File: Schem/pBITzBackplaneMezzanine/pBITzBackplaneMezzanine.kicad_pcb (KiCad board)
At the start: 4 copper layers, 139 x 130 mm, 54 parts, among them J1 USB3_A_Stacked, J2 Conn_01x04, J3 Conn_01x04, J4 10067847-001RLF, J5 FH69-60S-0.5SH, J6 pBITzBus, J7 FH69-60S-0.5SH, SW1 SW_Coded_SH-7030, SW2 SW_Coded_SH-7030, U1 FE1.1S-BSOP28BCN, U2 MAX3421EETJ_T, U3 CD74HC4050M96, U4 CD74HC4050M96, U5 74HC688, U6 74HC688, Y1 ABL-12.000MHZ-B2, Y2 ABL-12.000MHZ-B2

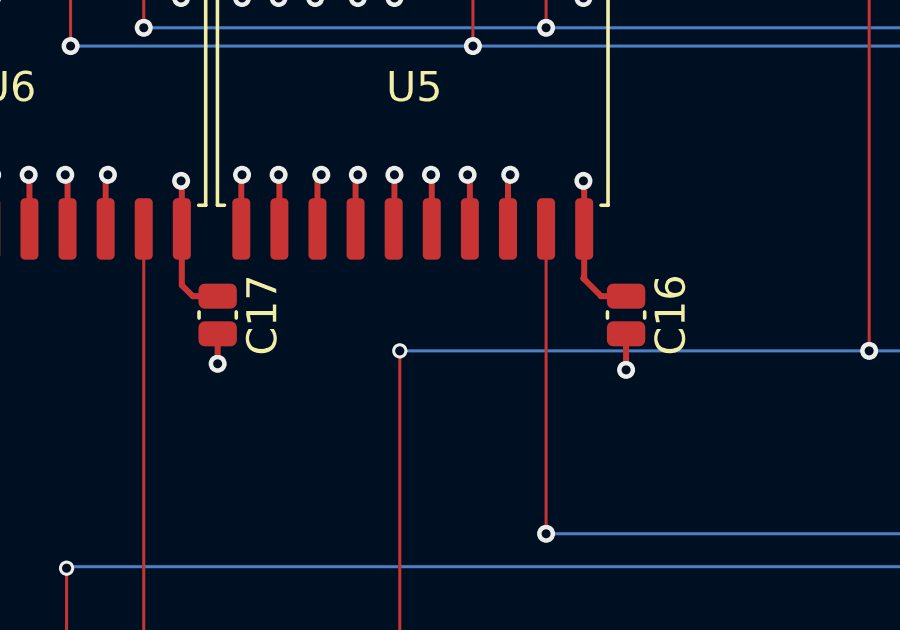
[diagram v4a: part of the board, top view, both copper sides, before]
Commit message: Small errors in BOM
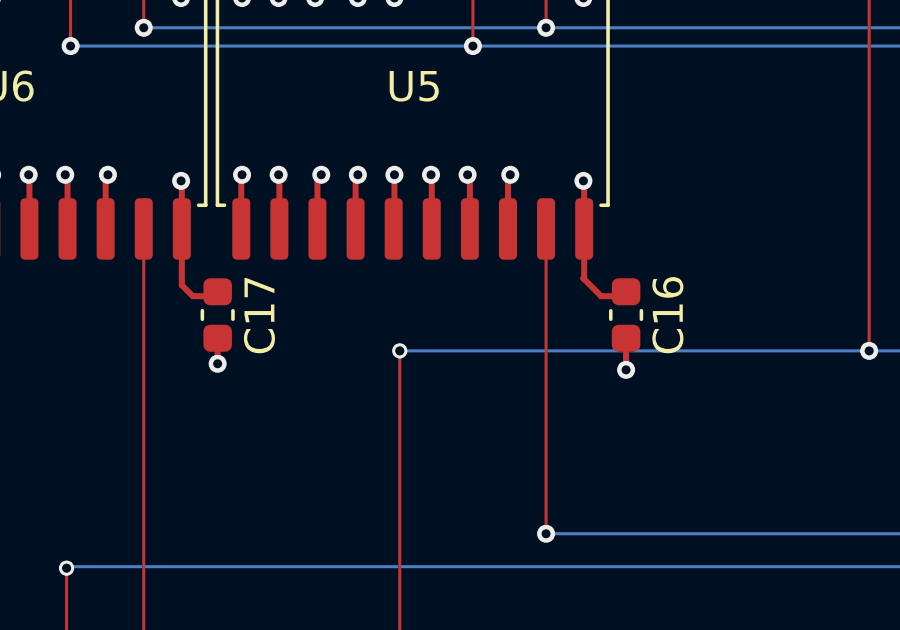
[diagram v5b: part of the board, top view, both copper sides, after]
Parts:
- C16, C17: footprint Capacitor_SMD:C_0504_1310Metric_Pad0.83x1.28mm_HandSolder -> Capacitor_SMD:C_0603_1608Metric
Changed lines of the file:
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@@
 		)
 	)
-	(footprint "Capacitor_SMD:C_0504_1310Metric_Pad0.83x1.28mm_HandSolder"
+	(footprint "Capacitor_SMD:C_0603_1608Metric"
 		(layer "F.Cu")
 		(at 273.747 177.5724 -90)
-		(descr "Capacitor SMD 0504 (1310 Metric), square (rectangular) end terminal, IPC-7351 nominal with elongated pad for handsoldering. (Body size source: IPC-SM-782 page 76, https://www.pcb-3d.com/wordpress/wp-content/uploads/ipc-sm-782a_amendment_1_and_2.pdf), generated with kicad-footprint-generator")
-		(tags "capacitor handsolder")
+		(descr "Capacitor SMD 0603 (1608 Metric), square (rectangular) end terminal, IPC-7351 nominal, (Body size source: IPC-SM-782 page 76, https://www.pcb-3d.com/wordpress/wp-content/uploads/ipc-sm-782a_amendment_1_and_2.pdf), generated with kicad-footprint-generator")
+		(tags "capacitor")
 		(property "Reference" "C17"
-			(at 0 -1.49 270)
+			(at 0 -1.43 270)
 			(layer "F.SilkS")
 			(effects
@@
 		)
 		(property "Value" "100n"
-			(at 0 1.49 270)
+			(at 0 1.43 270)
 			(layer "F.Fab")
 			(effects
@@
 				(font
 					(size 1.27 1.27)
+					(thickness 0.15)
+				)
+			)
+		)
+		(property "MANUFACTURER_PART_NUMBER" "C0603C104K5RACTU"
+			(at 0 0 270)
+			(unlocked yes)
+			(layer "F.Fab")
+			(hide yes)
+			(effects
+				(font
+					(size 1 1)
 					(thickness 0.15)
 				)
@@
 		(attr smd)
 		(fp_line
-			(start -0.101969 0.62)
-			(end 0.101969 0.62)
+			(start -0.14058 0.51)
+			(end 0.14058 0.51)
 			(stroke
 				(width 0.12)
@@
 		)
 		(fp_line
-			(start -0.101969 -0.62)
-			(end 0.101969 -0.62)
+			(start -0.14058 -0.51)
+			(end 0.14058 -0.51)
 			(stroke
 				(width 0.12)
@@
 		)
 		(fp_rect
-			(start -1.2 -0.79)
-			(end 1.2 0.79)
+			(start -1.48 -0.73)
+			(end 1.48 0.73)
 			(stroke
 				(width 0.05)
@@
 		)
 		(fp_rect
-			(start -0.585 -0.51)
-			(end 0.585 0.51)
+			(start -0.8 -0.4)
+			(end 0.8 0.4)
 			(stroke
 				(width 0.1)
@@
 			(effects
 				(font
-					(size 0.29 0.29)
-					(thickness 0.04)
+					(size 0.4 0.4)
+					(thickness 0.06)
 				)
 			)
 		)
 		(pad "1" smd roundrect
-			(at -0.6275 0 270)
-			(size 0.835 1.28)
+			(at -0.775 0 270)
+			(size 0.9 0.95)
 			(layers "F.Cu" "F.Mask" "F.Paste")
 			(roundrect_rratio 0.25)
@@
 		)
 		(pad "2" smd roundrect
-			(at 0.6275 0 270)
-			(size 0.835 1.28)
+			(at 0.775 0 270)
+			(size 0.9 0.95)
 			(layers "F.Cu" "F.Mask" "F.Paste")
 			(roundrect_rratio 0.25)
@@
 		)
 		(embedded_fonts no)
-		(model "${KICAD9_3DMODEL_DIR}/Capacitor_SMD.3dshapes/C_0504_1310Metric.step"
+		(model "${KICAD9_3DMODEL_DIR}/Capacitor_SMD.3dshapes/C_0603_1608Metric.step"
 			(offset
 				(xyz 0 0 0)
@@
 		)
 	)
-	(footprint "Capacitor_SMD:C_0504_1310Metric_Pad0.83x1.28mm_HandSolder"
+	(footprint "Capacitor_SMD:C_0603_1608Metric"
 		(layer "F.Cu")
 		(at 287.3614 177.5724 -90)
-		(descr "Capacitor SMD 0504 (1310 Metric), square (rectangular) end terminal, IPC-7351 nominal with elongated pad for handsoldering. (Body size source: IPC-SM-782 page 76, https://www.pcb-3d.com/wordpress/wp-content/uploads/ipc-sm-782a_amendment_1_and_2.pdf), generated with kicad-footprint-generator")
-		(tags "capacitor handsolder")
+		(descr "Capacitor SMD 0603 (1608 Metric), square (rectangular) end terminal, IPC-7351 nominal, (Body size source: IPC-SM-782 page 76, https://www.pcb-3d.com/wordpress/wp-content/uploads/ipc-sm-782a_amendment_1_and_2.pdf), generated with kicad-footprint-generator")
+		(tags "capacitor")
 		(property "Reference" "C16"
-			(at 0 -1.49 270)
+			(at 0 -1.43 270)
 			(layer "F.SilkS")
 			(effects
@@
 		)
 		(property "Value" "100n"
-			(at 0 1.49 270)
+			(at 0 1.43 270)
 			(layer "F.Fab")
 			(effects
@@
 				(font
 					(size 1.27 1.27)
+					(thickness 0.15)
+				)
+			)
+		)
+		(property "MANUFACTURER_PART_NUMBER" "C0603C104K5RACTU"
+			(at 0 0 270)
+			(unlocked yes)
+			(layer "F.Fab")
+			(hide yes)
+			(effects
+				(font
+					(size 1 1)
 					(thickness 0.15)
 				)
@@
 		(attr smd)
 		(fp_line
-			(start -0.101969 0.62)
-			(end 0.101969 0.62)
+			(start -0.14058 0.51)
+			(end 0.14058 0.51)
 			(stroke
 				(width 0.12)
@@
 		)
 		(fp_line
-			(start -0.101969 -0.62)
-			(end 0.101969 -0.62)
+			(start -0.14058 -0.51)
+			(end 0.14058 -0.51)
 			(stroke
 				(width 0.12)
@@
 		)
 		(fp_rect
-			(start -1.2 -0.79)
-			(end 1.2 0.79)
+			(start -1.48 -0.73)
+			(end 1.48 0.73)
 			(stroke
 				(width 0.05)
@@
 		)
 		(fp_rect
-			(start -0.585 -0.51)
-			(end 0.585 0.51)
+			(start -0.8 -0.4)
+			(end 0.8 0.4)
 			(stroke
 				(width 0.1)
@@
 			(effects
 				(font
-					(size 0.29 0.29)
-					(thickness 0.04)
+					(size 0.4 0.4)
+					(thickness 0.06)
 				)
 			)
 		)
 		(pad "1" smd roundrect
-			(at -0.6275 0 270)
-			(size 0.835 1.28)
+			(at -0.775 0 270)
+			(size 0.9 0.95)
 			(layers "F.Cu" "F.Mask" "F.Paste")
 			(roundrect_rratio 0.25)
@@
 		)
 		(pad "2" smd roundrect
-			(at 0.6275 0 270)
-			(size 0.835 1.28)
+			(at 0.775 0 270)
+			(size 0.9 0.95)
 			(layers "F.Cu" "F.Mask" "F.Paste")
 			(roundrect_rratio 0.25)
@@
 		)
 		(embedded_fonts no)
-		(model "${KICAD9_3DMODEL_DIR}/Capacitor_SMD.3dshapes/C_0504_1310Metric.step"
+		(model "${KICAD9_3DMODEL_DIR}/Capacitor_SMD.3dshapes/C_0603_1608Metric.step"
 			(offset
 				(xyz 0 0 0)

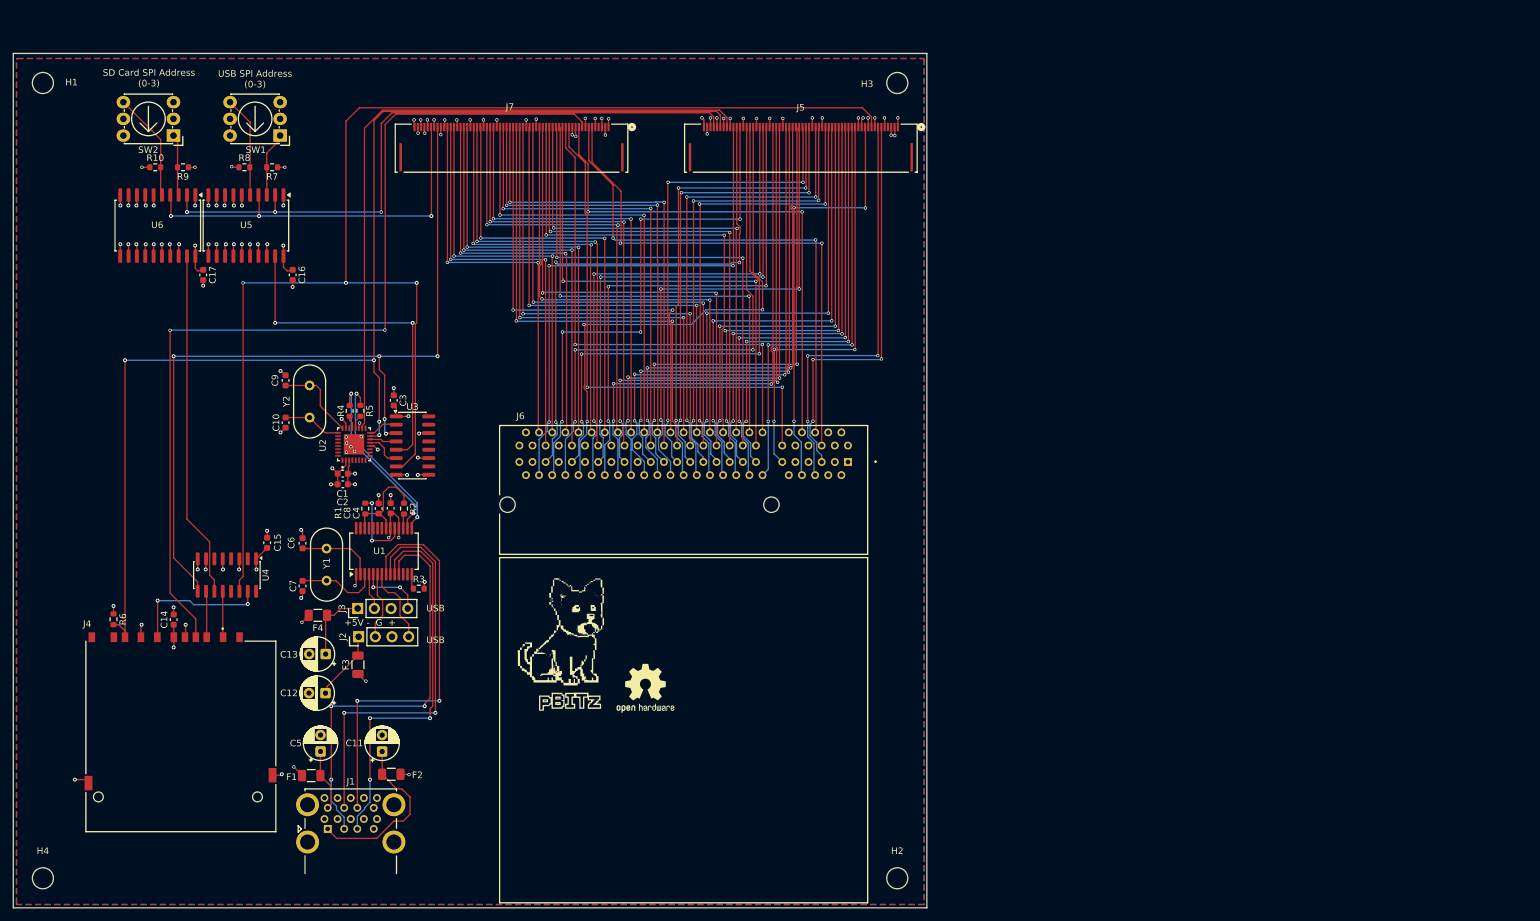
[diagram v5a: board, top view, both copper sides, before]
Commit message: Major rework:
- Updated the Mezzanine to remove the slot connector and move it to the main board (facing the back)
-    The removal of the slot allowed for the removal of the FPC connector, which was a
     major source of complexity. The mezzanine now only has the SD card and USB connectors,
     which are much cheaper and easier to work with.
- The mezzanine is now more compact and cheaper to souirce

- The main board sees the addition of the external slot connector (coming from the mezzanine)
- Added power led on the mother board for easier debugging and testing
- Removed the free floating resistors to replace them with resistor packs
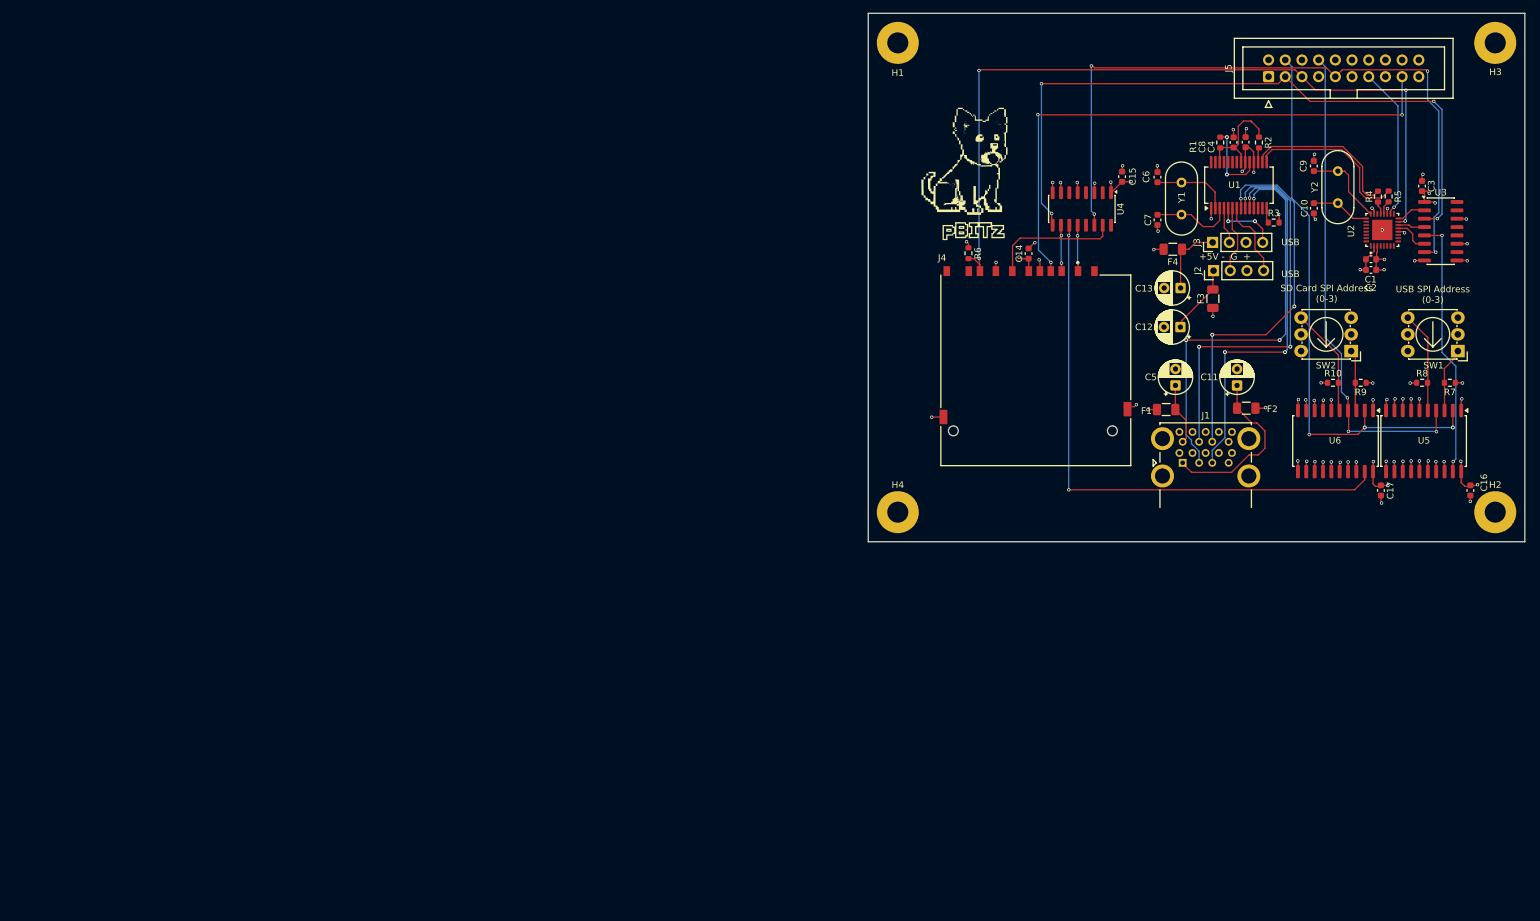
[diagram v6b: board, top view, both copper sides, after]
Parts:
- removed J6: pBITzBus, Footprints:SAMTEC_PCIE-098-02-X-D-RA
- removed J7: FH69-60S-0.5SH, Footprints:CONN60_FH69-60S_HIR
- removed REF**: OSHW-Logo2_9.8x8mm_SilkScreen, Symbol:OSHW-Logo2_9.8x8mm_SilkScreen
- H1, H2, H3, H4: footprint MountingHole:MountingHole_3.2mm_M3 -> MountingHole:MountingHole_3.2mm_M3_Pad
- J5: value FH69-60S-0.5SH -> Conn_02x10_Odd_Even; footprint Footprints:CONN60_FH69-60S_HIR -> Connector_IDC:IDC-Header_2x10_P2.54mm_Vertical
- moved R10 182.2 mm to (445.7, 194.0)
- moved R7 182.2 mm to (463.4, 194.0)
- moved SW1 182.2 mm to (464.6, 189.2)
- moved SW2 182.2 mm to (448.4, 189.2)
- moved U5 182.2 mm to (459.4, 202.8)
- moved U6 182.2 mm to (446.0, 202.8)
- moved C16 182.2 mm to (466.6, 210.4)
- moved C17 182.2 mm to (452.9, 210.4)
- moved R8 182.2 mm to (459.2, 194.0)
- moved R9 182.2 mm to (449.9, 194.0)
- moved C10 159.8 mm to (442.7, 167.4)
- moved C3 159.8 mm to (459.2, 164.0)
- moved C9 159.8 mm to (442.7, 161.0)
- moved R4 159.8 mm to (452.5, 165.6)
- moved R5 159.8 mm to (454.1, 165.6)
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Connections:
- J4 pad CD: /MezzanineConnector/SPI_CD -> /MezzanineConnector/~{SD_PRESENT}
- J5 pad 1: GND -> +5V
- J5 pad 11: /MezzanineConnector/PROG -> GND
- J5 pad 12: +3V3 -> unconnected-(J5-Pin_12-Pad12)
- J5 pad 13: +3V3 -> /MezzanineConnector/~{SPI_INT}
- J5 pad 14: /MezzanineConnector/CTRL_10 -> GND
- J5 pad 15: /MezzanineConnector/CTRL_11 -> GND
- J5 pad 16: /MezzanineConnector/CTRL_12 -> GND
- J5 pad 17: /MezzanineConnector/CTRL_13 -> /MezzanineConnector/~{SD_PRESENT}
- J5 pad 18: /MezzanineConnector/CTRL_14 -> GND
- J5 pad 19: /MezzanineConnector/CTRL_15 -> GND
- J5 pad 2: +5V -> +3V3
- J5 pad 20: /MezzanineConnector/CTRL_16 -> GND
- J5 pad 3: +5V -> /MezzanineConnector/MOSI
- J5 pad 4: unconnected-(J5-Pad4) -> /MezzanineConnector/SPI_CS0
- J5 pad 5: GND -> /MezzanineConnector/MISO
- J5 pad 6: /MezzanineConnector/CLK2 -> GND
- J5 pad 7: /MezzanineConnector/CLK3 -> GND
- J5 pad 8: GND -> /MezzanineConnector/SPI_CS1
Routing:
- net /MezzanineConnector/SPI_CD: track 144.2 -> 0.00 mm, vias 2 -> 0
- net /MezzanineConnector/SPI_CLK: track 210.9 -> 107.2 mm, vias 3 -> 4
- net /MezzanineConnector/~{SD_PRESENT}: track 0.00 -> 85.9 mm, vias 0 -> 3
- net /MezzanineConnector/A23: track 81.6 -> 0.00 mm, vias 3 -> 0
- net /MezzanineConnector/CLK0: track 81.0 -> 0.00 mm, vias 2 -> 0
- net /MezzanineConnector/A20: track 81.0 -> 0.00 mm, vias 3 -> 0
- net /MezzanineConnector/~{SPI_INT}: track 104.0 -> 23.2 mm, vias 0 -> 1
- net /MezzanineConnector/A21: track 80.6 -> 0.00 mm, vias 5 -> 0
- net /MezzanineConnector/A22: track 80.3 -> 0.00 mm, vias 3 -> 0
- net /MezzanineConnector/A18: track 80.2 -> 0.00 mm, vias 3 -> 0
- net /MezzanineConnector/CART: track 79.6 -> 0.00 mm, vias 2 -> 0
- net /MezzanineConnector/A19: track 79.4 -> 0.00 mm, vias 3 -> 0
- net /MezzanineConnector/~{RESET}: track 79.3 -> 0.00 mm, vias 2 -> 0
- net /MezzanineConnector/CLK1: track 78.8 -> 0.00 mm, vias 2 -> 0
- net /MezzanineConnector/A17: track 78.7 -> 0.00 mm, vias 3 -> 0
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- removed copper zone on B.Cu, net GND
- removed copper zone on F.Cu, net GND
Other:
- board size 139 x 130 mm -> 99.9 x 80.4 mm

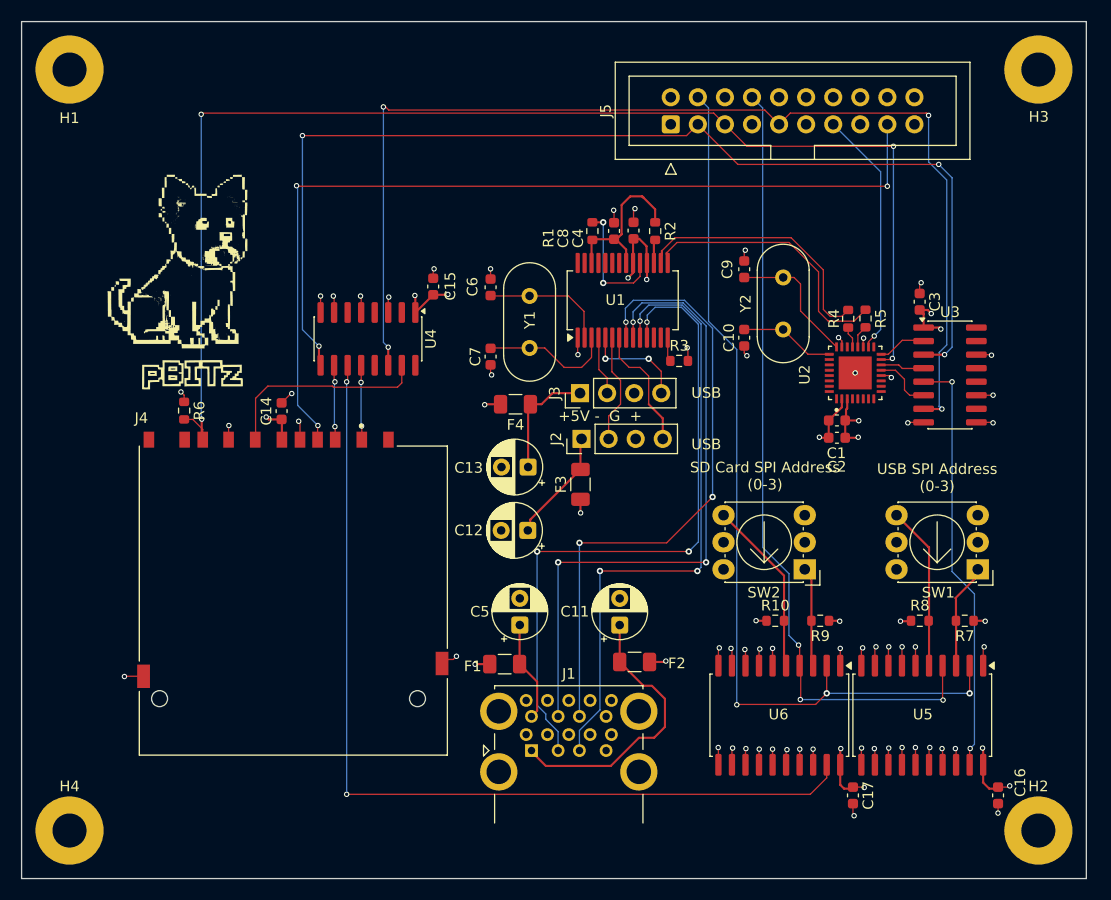
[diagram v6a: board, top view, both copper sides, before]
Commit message: Regenerated pictures, schematics, BOM files and production files for the mezzanine
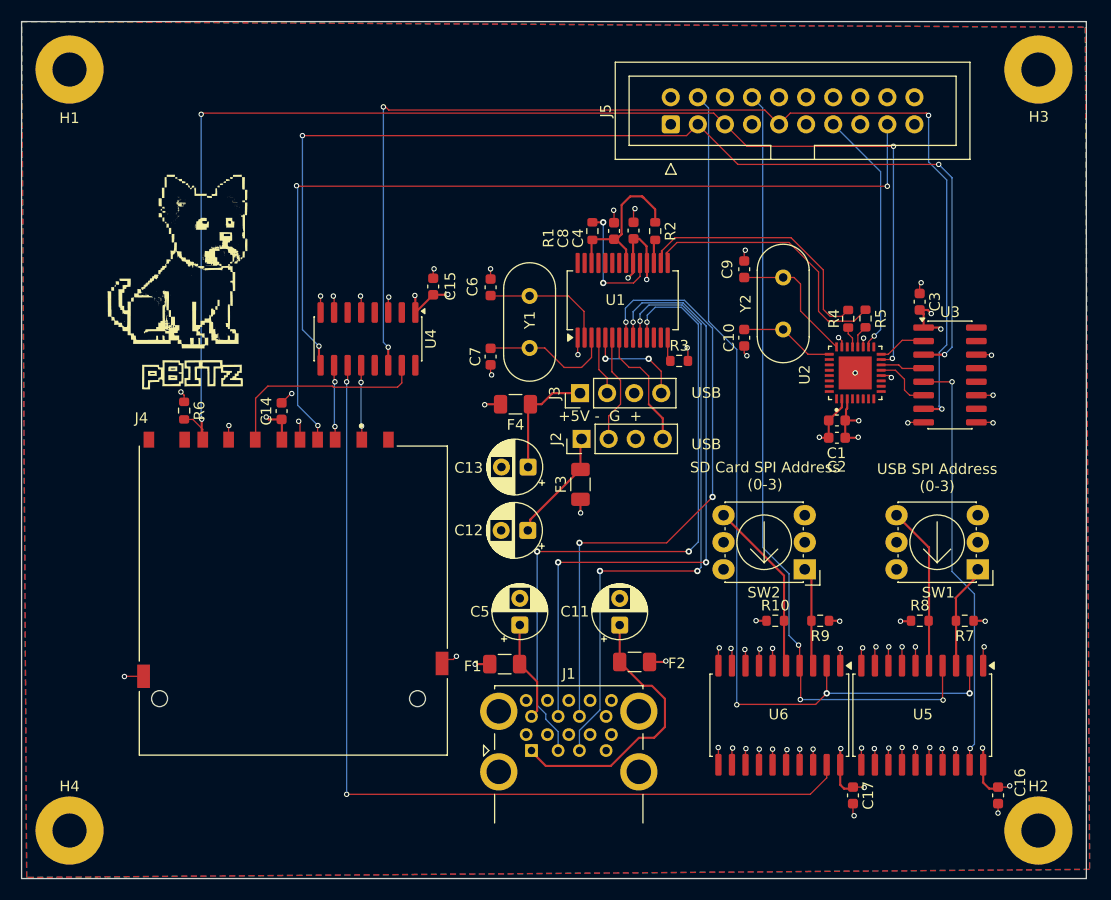
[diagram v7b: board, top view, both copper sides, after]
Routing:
- added copper zone on B.Cu, net GND
- added copper zone on F.Cu, net GND
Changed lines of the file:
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@@
+	(zone
+		(net "GND")
+		(layers "F.Cu" "B.Cu")
+		(hatch edge 0.5)
+		(priority 4)
+		(connect_pads
+			(clearance 0.5)
+		)
+		(min_thickness 0.25)
+		(fill yes
+			(thermal_gap 0.5)
+			(thermal_bridge_width 0.5)
+			(island_removal_mode 0)
+		)
+		(polygon
+			(pts
+				(xy 374.9364 137.762198) (xy 474.7364 138.29558) (xy 475.145349 217.304375) (xy 375.413545 218.062199)
+			)
+		)
+	)
 	(zone
 		(net "GND")
